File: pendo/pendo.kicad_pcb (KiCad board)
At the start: 4 copper layers, 24.5 x 94.8 mm, 28 parts, among them J1 M2, J2 M1, J3 Motor Vin, J4 Conn_ARM_JTAG_SWD_10, SW1 SW_Push, U1 STM32G431RBTx, U2 DRV8870DDA, U3 DRV8870DDA, U4 ESP32-C3-WROOM-02, U5 AP2112K-3.3

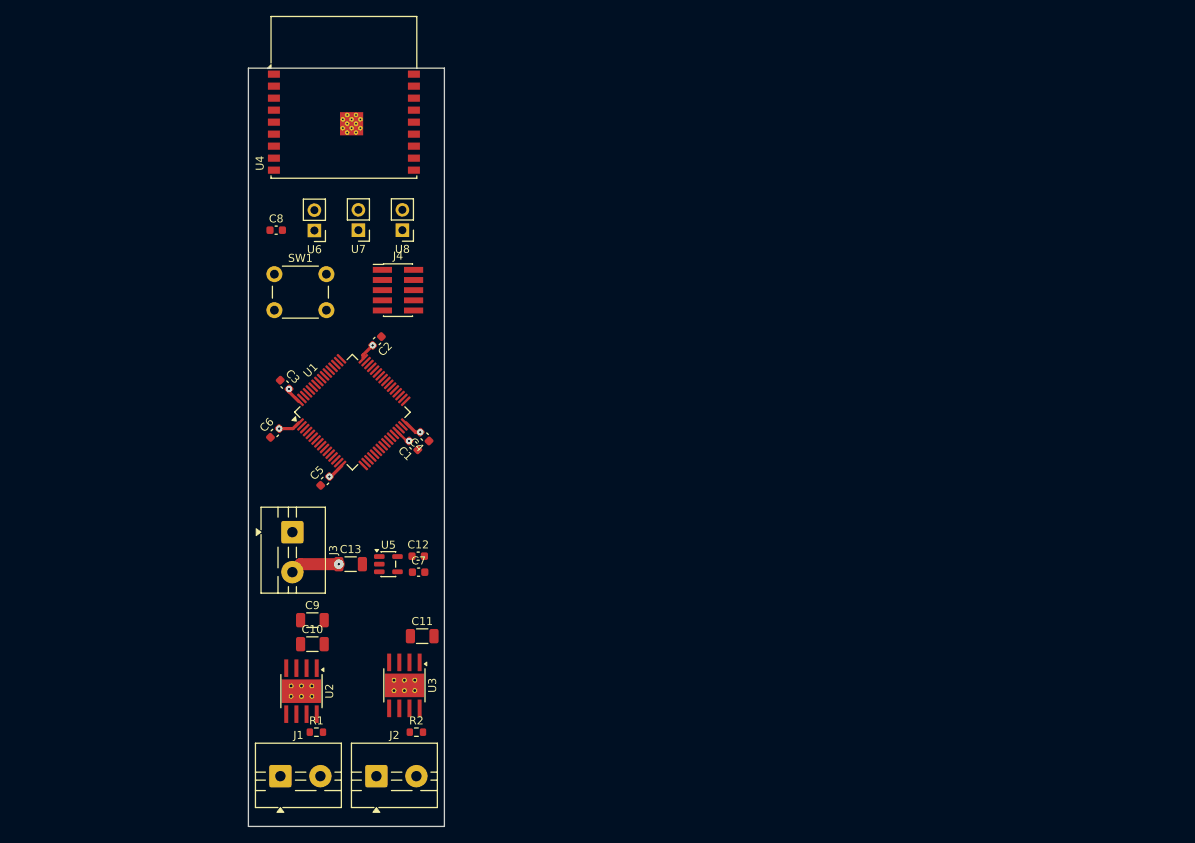
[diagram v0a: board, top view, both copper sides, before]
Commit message: started gerber redesign + update power components
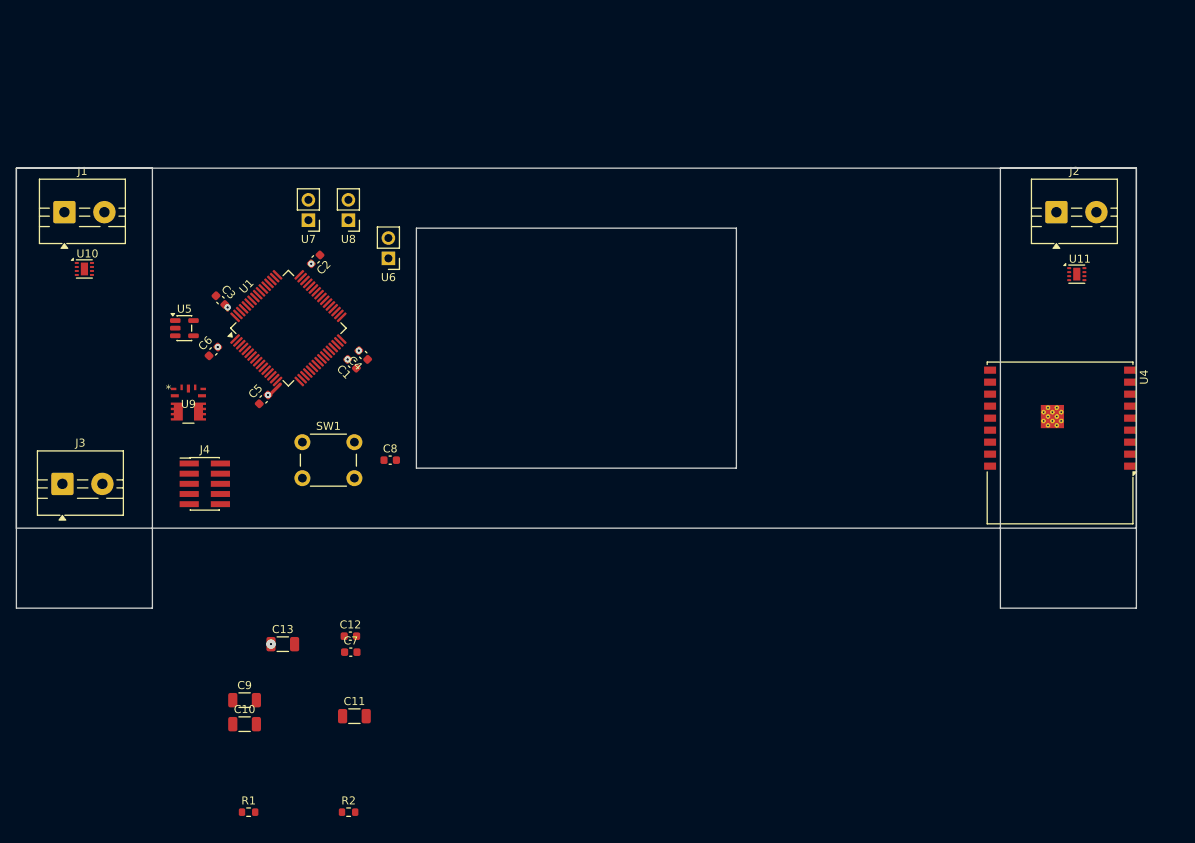
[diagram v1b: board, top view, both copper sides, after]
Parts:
- removed U2, U3: DRV8870DDA, Package_SO:Texas_HTSOP-8-1EP_3.9x4.9mm_P1.27mm_EP2.95x4.9mm_Mask2.4x3.1mm_ThermalVias
- added U10: DRV8231ADSG, Package_SON:WSON-8-1EP_2x2mm_P0.5mm_EP0.9x1.6mm, F.Cu at (100.0, 85.1)
- added U11: DRV8231ADSG, Package_SON:WSON-8-1EP_2x2mm_P0.5mm_EP0.9x1.6mm, F.Cu at (224.1, 85.8)
- added U9: RPX-2.5-CT, footprints:RPX-2.5, F.Cu at (113.0, 102.0)
- moved J2 110.4 mm to (221.5, 78.0)
- moved U4 96.9 mm to (222.0, 103.8), turned to 180 degrees
- moved J1 75.5 mm to (97.5, 78.0)
- moved U5 39.0 mm to (112.5, 92.5)
- moved J4 34.2 mm to (115.0, 112.0)
- moved C8 32.1 mm to (138.2, 109.0)
- moved J3 29.4 mm to (97.2, 112.0), turned to 0 degrees
- moved SW1 21.3 mm to (127.2, 106.8)
- moved C3 13.3 mm to (117.0, 89.0)
- moved U1 13.2 mm to (125.5, 92.5)
- moved C13 13.1 mm to (124.8, 132.0)
- moved C10 13.1 mm to (120.0, 142.0)
- moved C11 13.1 mm to (133.8, 141.0)
- moved C12 13.1 mm to (133.2, 131.0)
- moved C7 13.1 mm to (133.3, 133.0)
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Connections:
- C10 pad 1: +12V -> Net-(U10-VM)
- C11 pad 1: +12V -> Net-(U10-VM)
- C13 pad 1: +12V -> Net-(U10-VM)
- C9 pad 1: +12V -> Net-(U10-VM)
- J3 pad 2: +12V -> unconnected-(J3-Pin_2-Pad2)
- U5 pad 1: +12V -> Net-(U10-VM)
- U5 pad 3: +12V -> Net-(U10-VM)
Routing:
- net +3.3V: track 13.3 -> 2.75 mm
- net +12V: track 6.21 -> 0.00 mm, vias 1 -> 0
- net Net-(U10-VM): vias 0 -> 1
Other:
- board size 24.5 x 94.8 mm -> 140 x 55 mm

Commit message: cleaning up pendulum schematic
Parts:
- added U2: LSM6DS3, Package_LGA:LGA-14_3x2.5mm_P0.5mm_LayoutBorder3x4y, F.Cu at (200.1, 102.0)
- moved J3 94.9 mm to (186.0, 78.5)
- moved U7 41.7 mm to (149.0, 115.0)
- moved U9 39.9 mm to (142.9, 75.6)
- moved U8 37.8 mm to (144.5, 115.0)
- moved U6 34.6 mm to (153.0, 115.0)
- moved U5 30.1 mm to (137.4, 75.5)
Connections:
- net Net-(U1-PC0) renamed /TIM1_1
- net Net-(U1-PC1) renamed /TIM1_2
- net Net-(U1-PC2) renamed /TIM1_3
- net Net-(U1-PC3) renamed /TIM1_4
- C1 pad 2: +3.3V -> Net-(C1-Pad2)
- C10 pad 1: Net-(U10-VM) -> +12V
- C11 pad 1: Net-(U10-VM) -> +12V
- C13 pad 1: Net-(U10-VM) -> +5V
- C2 pad 2: +3.3V -> Net-(C1-Pad2)
- C3 pad 2: +3.3V -> Net-(C1-Pad2)
- C4 pad 2: +3.3V -> Net-(C1-Pad2)
- C5 pad 2: +3.3V -> Net-(C1-Pad2)
- C6 pad 2: +3.3V -> Net-(C1-Pad2)
- C7 pad 1: +3.3V -> Net-(C1-Pad2)
- C8 pad 1: Net-(J4-~{RESET}) -> GND
- C9 pad 1: Net-(U10-VM) -> +12V
- J4 pad 10: Net-(J4-~{RESET}) -> GND
- J4 pad 2: unconnected-(J4-SWDIO/TMS-Pad2) -> /JDB_SWDIO
- J4 pad 4: unconnected-(J4-SWCLK/TCK-Pad4) -> /JDB_SWCLK
- SW1 pad 1: Net-(J4-~{RESET}) -> GND
- U1 pad 14: unconnected-(U1-PA2-Pad14) -> /ESP32_RX
- U1 pad 17: unconnected-(U1-PA3-Pad17) -> /ESP32_TX
- U1 pad 7: Net-(J4-~{RESET}) -> GND
- U10 pad 5: Net-(U10-VM) -> +12V
- U11 pad 5: Net-(U10-VM) -> +12V
- U4 pad 11: unconnected-(U4-IO20/RXD-Pad11) -> /ESP32_RX
- U4 pad 12: unconnected-(U4-IO21/TXD-Pad12) -> /ESP32_TX
- U4 pad 15: unconnected-(U4-IO3-Pad15) -> /JDB_SWDIO
- U4 pad 16: unconnected-(U4-IO2-Pad16) -> /JDB_SWCLK
- U4 pad 3: unconnected-(U4-IO4-Pad3) -> GND
- U5 pad 1: Net-(U10-VM) -> +5V
- U5 pad 3: Net-(U10-VM) -> +5V
- U9 pad 3: +3.3V -> +5V
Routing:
- net Net-(C1-Pad2): track 0.00 -> 2.75 mm, vias 0 -> 6
- net +3.3V: track 2.75 -> 0.00 mm, vias 6 -> 0
- net Net-(U10-VM): vias 1 -> 0
- net +5V: vias 0 -> 1

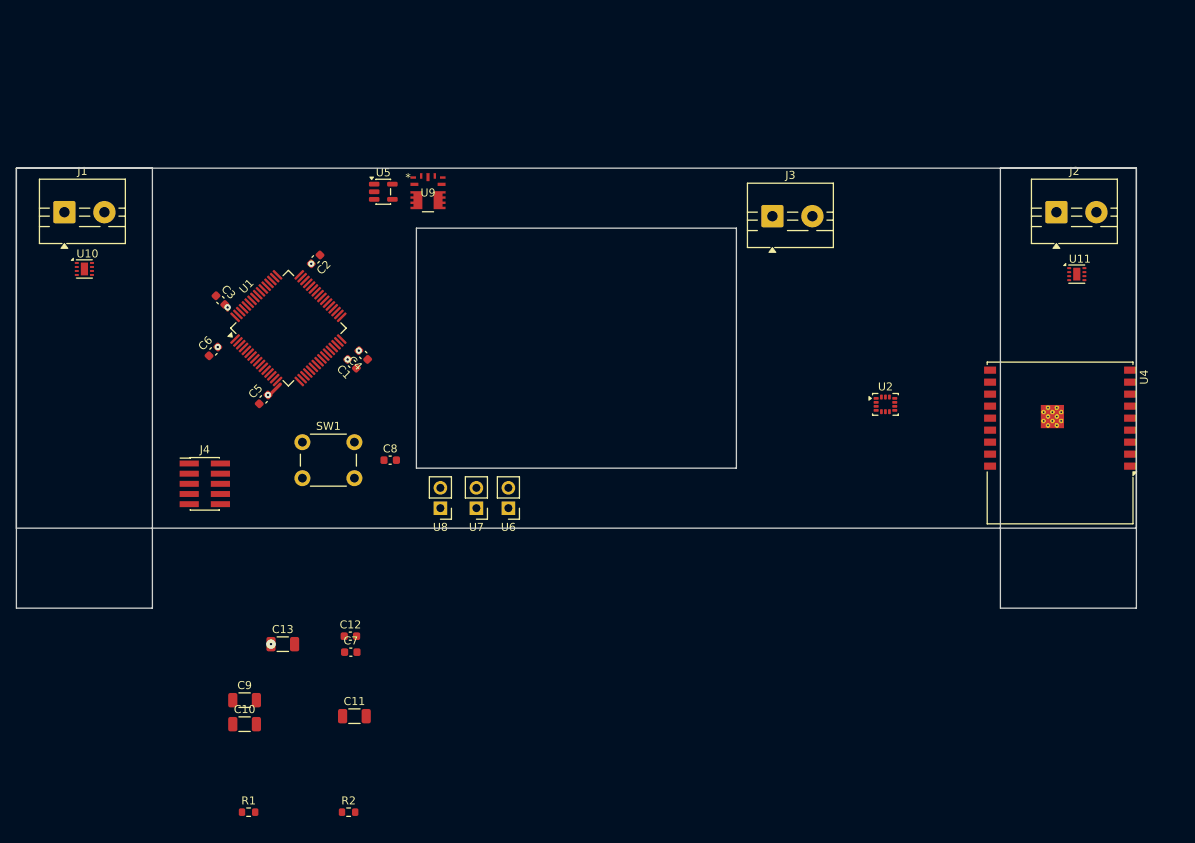
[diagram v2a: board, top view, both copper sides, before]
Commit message: added planes and almost finished routing
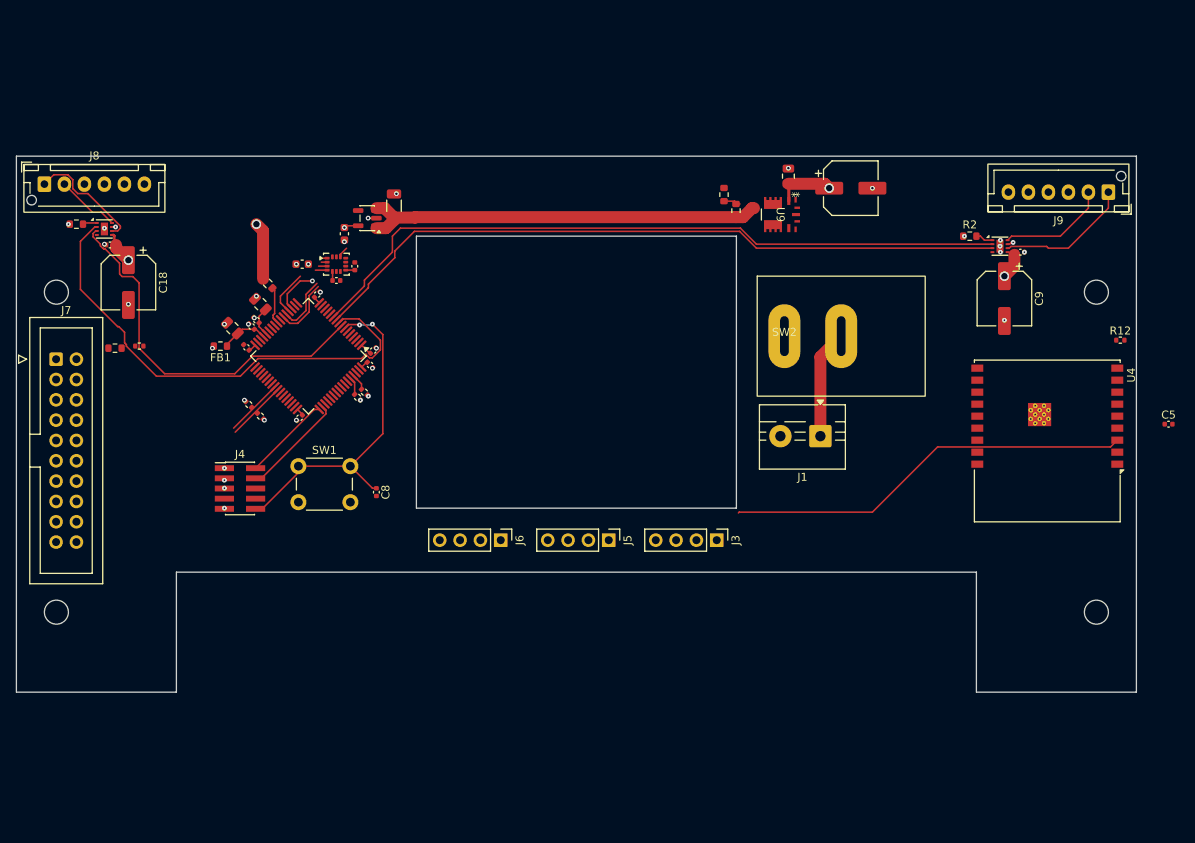
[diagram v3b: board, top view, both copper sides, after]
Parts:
- removed J2: M1, TerminalBlock:TerminalBlock_MaiXu_MX126-5.0-02P_1x02_P5.00mm
- removed U6, U7, U8: ~, Connector_PinHeader_2.54mm:PinHeader_1x02_P2.54mm_Vertical
- added C14: 10u, Capacitor_SMD:C_0805_2012Metric, F.Cu at (188.0, 73.5)
- added C15: 100u, Capacitor_SMD:CP_Elec_6.3x7.7, F.Cu at (195.8, 75.0)
- added C16: 1u, Capacitor_SMD:C_0402_1005Metric, F.Cu at (131.5, 86.5)
- added C17: 1u, Capacitor_SMD:C_0402_1005Metric, F.Cu at (133.8, 84.8)
- added C18: 47u, Capacitor_SMD:CP_Elec_6.3x5.4, F.Cu at (105.5, 86.8)
- added C19: 10u, Capacitor_SMD:C_0805_2012Metric, F.Cu at (118.5, 92.5)
- added C20: 1u, Capacitor_SMD:C_0402_1005Metric, F.Cu at (121.5, 91.5)
- added C21: 10u, Capacitor_SMD:C_0805_2012Metric, F.Cu at (122.0, 89.5)
- added C22: 1u, Capacitor_SMD:C_0402_1005Metric, F.Cu at (120.9, 92.3)
- added FB1: FerriteBead_Small, Resistor_SMD:R_0603_1608Metric, F.Cu at (117.0, 94.7)
- added J5: Conn_01x04_Pin, Connector_PinHeader_2.54mm:PinHeader_1x04_P2.54mm_Vertical, F.Cu at (165.5, 119.0)
- added J6: Conn_01x04_Pin, Connector_PinHeader_2.54mm:PinHeader_1x04_P2.54mm_Vertical, F.Cu at (152.0, 119.0)
- added J7: Conn_02x10_Odd_Even, Connector_IDC:IDC-Header_2x10_P2.54mm_Vertical, F.Cu at (96.5, 96.4)
- added J8: Conn_01x06_Pin, Connector_JST:JST_XH_B6B-XH-AM_1x06_P2.50mm_Vertical, F.Cu at (95.0, 74.5)
- added J9: Conn_01x06_Pin, Connector_JST:JST_XH_B6B-XH-AM_1x06_P2.50mm_Vertical, F.Cu at (228.0, 75.5)
- added R10: 4.7k, Resistor_SMD:R_0402_1005Metric, F.Cu at (135.0, 100.5)
- added R11: 4.7k, Resistor_SMD:R_0402_1005Metric, F.Cu at (134.1, 101.1)
- added R12: 10k, Resistor_SMD:R_0402_1005Metric, F.Cu at (229.5, 94.0)
- added R3: 10k, Resistor_SMD:R_0603_1608Metric, F.Cu at (122.9, 86.9)
- added R4: 10k, Resistor_SMD:R_0603_1608Metric, F.Cu at (181.4, 77.8)
- added R5: 3.3k, Resistor_SMD:R_0603_1608Metric, F.Cu at (103.8, 95.0)
- added R6: 1.37k, Resistor_SMD:R_0603_1608Metric, F.Cu at (179.9, 75.8)
- added R7: 10k, Resistor_SMD:R_0402_1005Metric, F.Cu at (106.9, 94.7)
- added R8: 4.7k, Resistor_SMD:R_0402_1005Metric, F.Cu at (120.5, 102.0)
- added R9: 4.7k, Resistor_SMD:R_0402_1005Metric, F.Cu at (122.0, 103.5)
- added SW2: SW_SPST, jlc:SWITCH HIGH VOLTAGE, F.Cu at (187.5, 93.5)
- C1, C2, C3, C4, C5, C6: value 0.1u -> 1u; footprint Capacitor_SMD:C_0603_1608Metric -> Capacitor_SMD:C_0402_1005Metric
- C10, C11: value 0.1u -> 1u; footprint Capacitor_SMD:C_1206_3216Metric -> Capacitor_SMD:C_0402_1005Metric
- C8: footprint Capacitor_SMD:C_0603_1608Metric -> Capacitor_SMD:C_0402_1005Metric
- C9: footprint Capacitor_SMD:C_1206_3216Metric -> Capacitor_SMD:CP_Elec_6.3x5.4
- J1: value M2 -> Screw_Terminal_01x02
- J3: value Motor Vin -> Conn_01x04_Pin; footprint TerminalBlock:TerminalBlock_MaiXu_MX126-5.0-02P_1x02_P5.00mm -> Connector_PinHeader_2.54mm:PinHeader_1x04_P2.54mm_Vertical
- R1, R2: value 0.2 -> 1.5k
- moved C5 113.2 mm to (235.5, 104.5), turned to 0 degrees
- moved C9 107.4 mm to (215.0, 88.8), turned to -90 degrees
- moved R2 105.9 mm to (210.7, 81.0)
- moved C11 101.5 mm to (217.0, 83.0), turned to 180 degrees
- moved J1 98.6 mm to (192.0, 106.0), turned to 180 degrees
- moved R1 76.6 mm to (99.0, 79.5)
- moved U2 70.8 mm to (131.5, 84.5)
- moved C10 62.2 mm to (103.2, 82.1)
- moved C13 56.5 mm to (138.7, 77.2), turned to 90 degrees
- moved C12 50.3 mm to (132.5, 80.7), turned to -90 degrees
- moved C7 48.9 mm to (127.2, 84.5), turned to 180 degrees
- moved U9 44.1 mm to (187.0, 78.3), turned to -90 degrees
- moved J3 41.1 mm to (179.0, 119.0), turned to -90 degrees
- moved C4 14.6 mm to (120.2, 94.9), turned to -45 degrees
- moved C6 13.6 mm to (126.9, 103.7)
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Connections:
- C1 pad 2: Net-(C1-Pad2) -> +3.3V
- C10 pad 1: +12V -> GND
- C10 pad 2: GND -> +12V
- C11 pad 1: +12V -> GND
- C11 pad 2: GND -> +12V
- C2 pad 2: Net-(C1-Pad2) -> +3.3V
- C3 pad 2: Net-(C1-Pad2) -> +3.3V
- C4 pad 2: Net-(C1-Pad2) -> +3.3V
- C5 pad 1: GND -> Net-(U4-EN)
- C5 pad 2: Net-(C1-Pad2) -> GND
- C6 pad 2: Net-(C1-Pad2) -> +3.3V
- C7 pad 1: Net-(C1-Pad2) -> +3.3V
- C8 pad 1: GND -> /JDB_RESET
- J1 pad 2: Net-(J1-Pin_2) -> GND
- J3 pad 2: unconnected-(J3-Pin_2-Pad2) -> +3.3V
- J4 pad 10: GND -> /JDB_RESET
- R1 pad 1: Net-(U10-IPROPI) -> GND
- R1 pad 2: GND -> /VPROPI1
- R2 pad 1: Net-(U11-IPROPI) -> GND
- R2 pad 2: GND -> /VPROPI2
- SW1 pad 1: GND -> /JDB_RESET
- U1 pad 12: unconnected-(U1-PA0-Pad12) -> /ENC1A
- U1 pad 13: unconnected-(U1-PA1-Pad13) -> /ENC1B
- U1 pad 18: unconnected-(U1-PA4-Pad18) -> /ENC2B
- U1 pad 19: unconnected-(U1-PA5-Pad19) -> /SPI1_SCK
- U1 pad 20: unconnected-(U1-PA6-Pad20) -> /SPI1_MISO
- U1 pad 21: unconnected-(U1-PA7-Pad21) -> /SPI1_MOSI
- U1 pad 22: unconnected-(U1-PC4-Pad22) -> /IMU_INT
- U1 pad 24: unconnected-(U1-PB0-Pad24) -> /VBAT_PROTECT
- U1 pad 25: unconnected-(U1-PB1-Pad25) -> /VPROPI1
- U1 pad 26: unconnected-(U1-PB2-Pad26) -> /VPROPI2
- U1 pad 28: unconnected-(U1-VREF+-Pad28) -> +3.3VA
- U1 pad 29: +3.3V -> +3.3VA
- U1 pad 30: unconnected-(U1-PB10-Pad30) -> /SPI1_GP_CS2
- U1 pad 33: unconnected-(U1-PB11-Pad33) -> /PB11
- U1 pad 34: unconnected-(U1-PB12-Pad34) -> /PB12
- U1 pad 35: unconnected-(U1-PB13-Pad35) -> /E_STOP
- U1 pad 38: unconnected-(U1-PC6-Pad38) -> /ENC2A
- U1 pad 40: Net-(U1-PC8) -> /I2C3_SCL
- U1 pad 41: Net-(U1-PC9) -> /I2C3_SDA
- U1 pad 42: unconnected-(U1-PA8-Pad42) -> /IMU_CS
- U1 pad 49: unconnected-(U1-PA13-Pad49) -> /JDB_SWDIO
- U1 pad 50: unconnected-(U1-PA14-Pad50) -> /JDB_SWCLK
- U1 pad 52: unconnected-(U1-PC10-Pad52) -> /USART3_TX
- U1 pad 53: unconnected-(U1-PC11-Pad53) -> /USART3_RX
- U1 pad 60: unconnected-(U1-PB7-Pad60) -> /I2C1_SDA
- U1 pad 61: unconnected-(U1-PB8-Pad61) -> /I2C1_SCL
- U1 pad 62: unconnected-(U1-PB9-Pad62) -> /SPI1_GP_CS1
- U1 pad 7: GND -> /JDB_RESET
- U10 pad 1: Net-(U10-IPROPI) -> /VPROPI1
- U10 pad 6: Net-(J1-Pin_1) -> /M1+
- U10 pad 8: Net-(J1-Pin_2) -> /M1-
- U11 pad 1: Net-(U11-IPROPI) -> /VPROPI2
- U11 pad 6: Net-(J2-Pin_1) -> /M2+
- U11 pad 8: Net-(J2-Pin_2) -> /M2-
- U2 pad 1: unconnected-(U2-SDO/SA0-Pad1) -> /SPI1_MISO
- U2 pad 12: unconnected-(U2-CS-Pad12) -> /IMU_CS
- U2 pad 2: unconnected-(U2-SDX-Pad2) -> /SPI1_MOSI
- U2 pad 3: unconnected-(U2-SCX-Pad3) -> /SPI1_SCK
- U2 pad 4: unconnected-(U2-INT1-Pad4) -> /IMU_INT
- U2 pad 5: unconnected-(U2-VDDIO-Pad5) -> +3.3V
- U2 pad 6: Net-(U2-GND-Pad6) -> GND
- U2 pad 7: Net-(U2-GND-Pad6) -> GND
- U2 pad 8: unconnected-(U2-VDD-Pad8) -> +3.3V
- U4 pad 2: unconnected-(U4-EN-Pad2) -> Net-(U4-EN)
- U4 pad 3: GND -> /JDB_RESET
- U9 pad 9: Net-(U9-CTRL) -> unconnected-(U9-CTRL-Pad9)
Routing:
- net /JDB_RESET: track 0.00 -> 93.7 mm, vias 0 -> 2
- net /TIM1_4: track 0.00 -> 89.4 mm
- net /TIM1_3: track 0.00 -> 88.2 mm
- net /TIM1_2: track 0.00 -> 61.1 mm
- net +5V: track 0.00 -> 51.1 mm, vias 1 -> 0
- net /TIM1_1: track 0.00 -> 47.4 mm
- net +12V: track 0.00 -> 21.9 mm, vias 0 -> 4
- net /M2+: track 0.00 -> 16.9 mm
- net /M1+: track 0.00 -> 14.8 mm
- net /M2-: track 0.00 -> 13.8 mm
- net Net-(J1-Pin_1): track 0.00 -> 13.6 mm
- net /JDB_SWCLK: track 0.00 -> 13.2 mm
- net /JDB_SWDIO: track 0.00 -> 11.0 mm
- net +3.3V: track 0.00 -> 10.4 mm, vias 0 -> 8
- net +3.3VA: track 0.00 -> 9.74 mm
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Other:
- board size 140 x 55 mm -> 140 x 67 mm
